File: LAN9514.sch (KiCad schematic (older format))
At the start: 45 parts, among them J1 RJ45-TRANSFO-2, P1 USB_2.0_Connector, U2 LAN9514, U3 MIC2026, U5 93LC66, Y1 25MHz

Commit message: review and discussion done
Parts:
- J1: symbol mechanical-connectors:RJ45-TRANSFO-2 -> pocketbeaglebase-rescue:RJ45-TRANSFO-2-mechanical-connectors
- P1: symbol usb_connector_header:USB_2.0_Connector -> pocketbeaglebase-rescue:USB_2.0_Connector-usb_connector_header
- U2: symbol IC_controller_Ethernet:LAN9514 -> pocketbeaglebase-rescue:LAN9514-IC_controller_Ethernet
- U3: symbol IC_loadswitch:MIC2026 -> pocketbeaglebase-rescue:MIC2026-IC_loadswitch
- U5: symbol IC_memory_flash:93LC66 -> pocketbeaglebase-rescue:93LC66-IC_memory_flash
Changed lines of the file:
@@
 $EndDescr
 $Comp
-L IC_controller_Ethernet:LAN9514 U2
+L pocketbeaglebase-rescue:LAN9514-IC_controller_Ethernet U2
 U 1 1 5FC3B911
 P 2250 2700
@@
 $EndComp
 $Comp
-L IC_controller_Ethernet:LAN9514 U2
+L pocketbeaglebase-rescue:LAN9514-IC_controller_Ethernet U2
 U 2 1 5FC3CBF0
 P 2000 6200
@@
 	1850 1400 1850 1300
 $Comp
-L IC_loadswitch:MIC2026 U3
+L pocketbeaglebase-rescue:MIC2026-IC_loadswitch U3
 U 1 1 5FC814BF
 P 5450 1850
@@
 $EndComp
 $Comp
-L usb_connector_header:USB_2.0_Connector P1
+L pocketbeaglebase-rescue:USB_2.0_Connector-usb_connector_header P1
 U 1 1 5FDC06C1
 P 9200 1850
@@
 $EndComp
 $Comp
-L IC_memory_flash:93LC66 U5
+L pocketbeaglebase-rescue:93LC66-IC_memory_flash U5
 U 1 1 5FD60BAB
 P 5300 7200
@@
 nPWR3
 $Comp
-L mechanical-connectors:RJ45-TRANSFO-2 J1
+L pocketbeaglebase-rescue:RJ45-TRANSFO-2-mechanical-connectors J1
 U 1 1 5FCFD3AD
 P 10250 5250
@@
 U 1 1 5FFD6ECD
 P 1150 5600
-F 0 "R1" V 1100 5500 50  0000 C CNN
+F 0 "R1" V 1100 5450 50  0000 C CNN
 F 1 "10k" V 1100 5750 50  0000 C CNN
 F 2 "resistors:R_0603" H 1150 5450 50  0001 C CNN

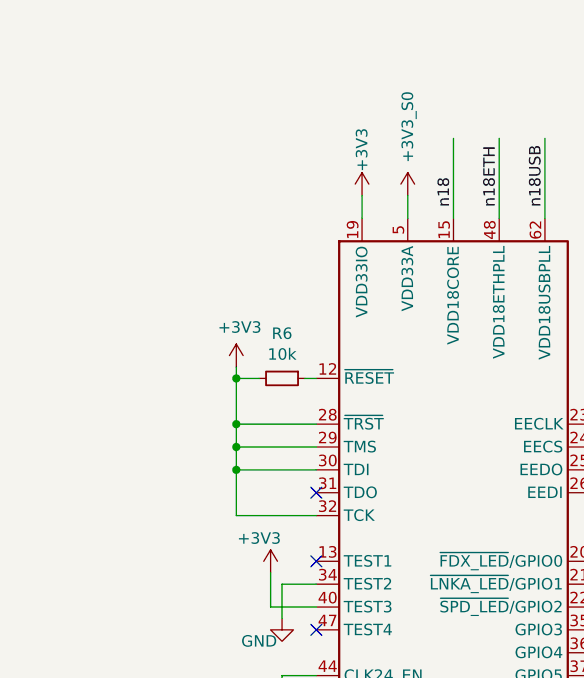
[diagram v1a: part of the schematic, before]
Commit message: added can bus
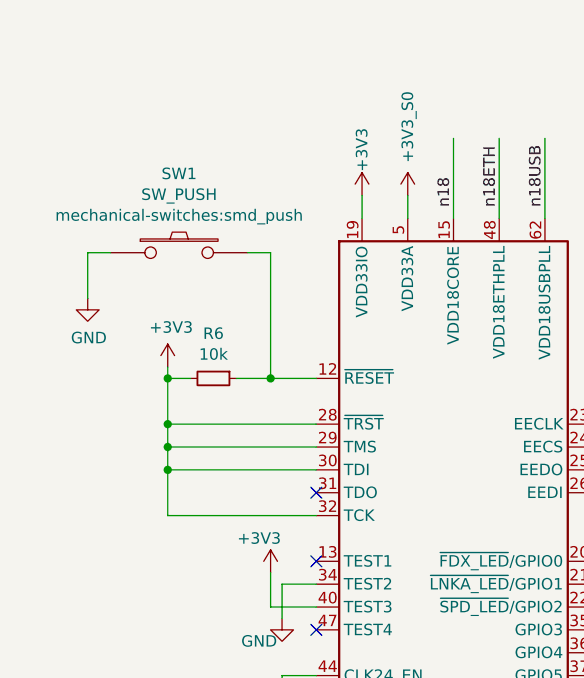
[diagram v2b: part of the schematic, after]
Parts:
- added SW1: SW_PUSH, mechanical-switches:smd_push, symbol devices:SW_PUSH
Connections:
- wire segments 233 -> 238
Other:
- moved on the sheet: R6
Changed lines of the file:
@@
 L devices:R_0603 R6
 U 1 1 5FC3DF7F
-P 1500 2100
-F 0 "R6" V 1304 2100 50  0000 C CNN
-F 1 "10k" V 1395 2100 50  0000 C CNN
-F 2 "resistors:R_0603" H 1500 1950 50  0001 C CNN
-F 3 "" H 1500 2100 50  0000 C CNN
-	1    1500 2100
+P 1200 2100
+F 0 "R6" V 1004 2100 50  0000 C CNN
+F 1 "10k" V 1095 2100 50  0000 C CNN
+F 2 "resistors:R_0603" H 1200 1950 50  0001 C CNN
+F 3 "" H 1200 2100 50  0000 C CNN
+	1    1200 2100
 	0    1    1    0
 $EndComp
@@
 L power-supply:+3V3 #PWR0101
 U 1 1 5FC3E6A0
-P 1300 2050
-F 0 "#PWR0101" H 1300 1900 50  0001 C CNN
-F 1 "+3V3" H 1315 2223 50  0000 C CNN
-F 2 "" H 1300 2050 50  0000 C CNN
-F 3 "" H 1300 2050 50  0000 C CNN
-	1    1300 2050
-	1    0    0    -1
-$EndComp
-Wire Wire Line
-	1650 2700 1300 2700
-Wire Wire Line
-	1300 2700 1300 2500
-Wire Wire Line
-	1650 2500 1300 2500
-Connection ~ 1300 2500
-Wire Wire Line
-	1300 2500 1300 2400
-Wire Wire Line
-	1650 2400 1300 2400
-Connection ~ 1300 2400
-Wire Wire Line
-	1300 2400 1300 2300
-Wire Wire Line
-	1650 2300 1300 2300
-Connection ~ 1300 2300
-Wire Wire Line
-	1300 2300 1300 2100
-Wire Wire Line
-	1650 2100 1600 2100
-Wire Wire Line
-	1400 2100 1300 2100
-Connection ~ 1300 2100
-Wire Wire Line
-	1300 2100 1300 2050
+P 1000 2050
+F 0 "#PWR0101" H 1000 1900 50  0001 C CNN
+F 1 "+3V3" H 1015 2223 50  0000 C CNN
+F 2 "" H 1000 2050 50  0000 C CNN
+F 3 "" H 1000 2050 50  0000 C CNN
+	1    1000 2050
+	1    0    0    -1
+$EndComp
+Wire Wire Line
+	1650 2700 1000 2700
+Wire Wire Line
+	1000 2700 1000 2500
+Wire Wire Line
+	1650 2500 1000 2500
+Connection ~ 1000 2500
+Wire Wire Line
+	1000 2500 1000 2400
+Wire Wire Line
+	1650 2400 1000 2400
+Connection ~ 1000 2400
+Wire Wire Line
+	1000 2400 1000 2300
+Wire Wire Line
+	1650 2300 1000 2300
+Connection ~ 1000 2300
+Wire Wire Line
+	1000 2300 1000 2100
+Wire Wire Line
+	1650 2100 1450 2100
+Wire Wire Line
+	1100 2100 1000 2100
+Connection ~ 1000 2100
+Wire Wire Line
+	1000 2100 1000 2050
 Wire Wire Line
 	1650 3000 1500 3000
@@
 	1    0    0    -1
 $EndComp
+$Comp
+L devices:SW_PUSH SW1
+U 1 1 5FDC5CF9
+P 1050 1550
+F 0 "SW1" H 1050 1895 50  0000 C CNN
+F 1 "SW_PUSH" H 1050 1804 50  0000 C CNN
+F 2 "mechanical-switches:smd_push" H 1050 1713 50  0000 C CNN
+F 3 "" H 1050 1550 50  0000 C CNN
+	1    1050 1550
+	1    0    0    -1
+$EndComp
+Wire Wire Line
+	1350 1550 1450 1550
+Wire Wire Line
+	1450 1550 1450 2100
+Connection ~ 1450 2100
+Wire Wire Line
+	1450 2100 1300 2100
+Wire Wire Line
+	750  1550 650  1550
+Wire Wire Line
+	650  1550 650  1750
+$Comp
+L power-supply:GND #PWR0156
+U 1 1 5FDE47CB
+P 650 1750
+F 0 "#PWR0156" H 650 1500 50  0001 C CNN
+F 1 "GND" H 655 1577 50  0000 C CNN
+F 2 "" H 650 1750 50  0000 C CNN
+F 3 "" H 650 1750 50  0000 C CNN
+	1    650  1750
+	1    0    0    -1
+$EndComp

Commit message: finally
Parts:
- Y1: footprint crystals:Crystal_SMD_0603_4Pads -> crystals:Crystal_SMD_5x3.2mm_4Pad
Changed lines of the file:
@@
 F 0 "Y1" H 1150 4100 50  0000 C CNN
 F 1 "25MHz" H 1350 4100 50  0000 C CNN
-F 2 "crystals:Crystal_SMD_0603_4Pads" H 1300 3800 50  0001 C CNN
+F 2 "crystals:Crystal_SMD_5x3.2mm_4Pad" H 1300 3800 50  0001 C CNN
 F 3 "" H 1300 4000 50  0000 C CNN
 	1    1300 4000
